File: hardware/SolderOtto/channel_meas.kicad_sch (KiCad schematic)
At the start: 66 parts, among them Q901 BC847A, Q902 BC858B, Q903 BC847A, U901 OPA202, U902 LM358B, U903 74hc4053, U904 OPA202, U905 OPA202

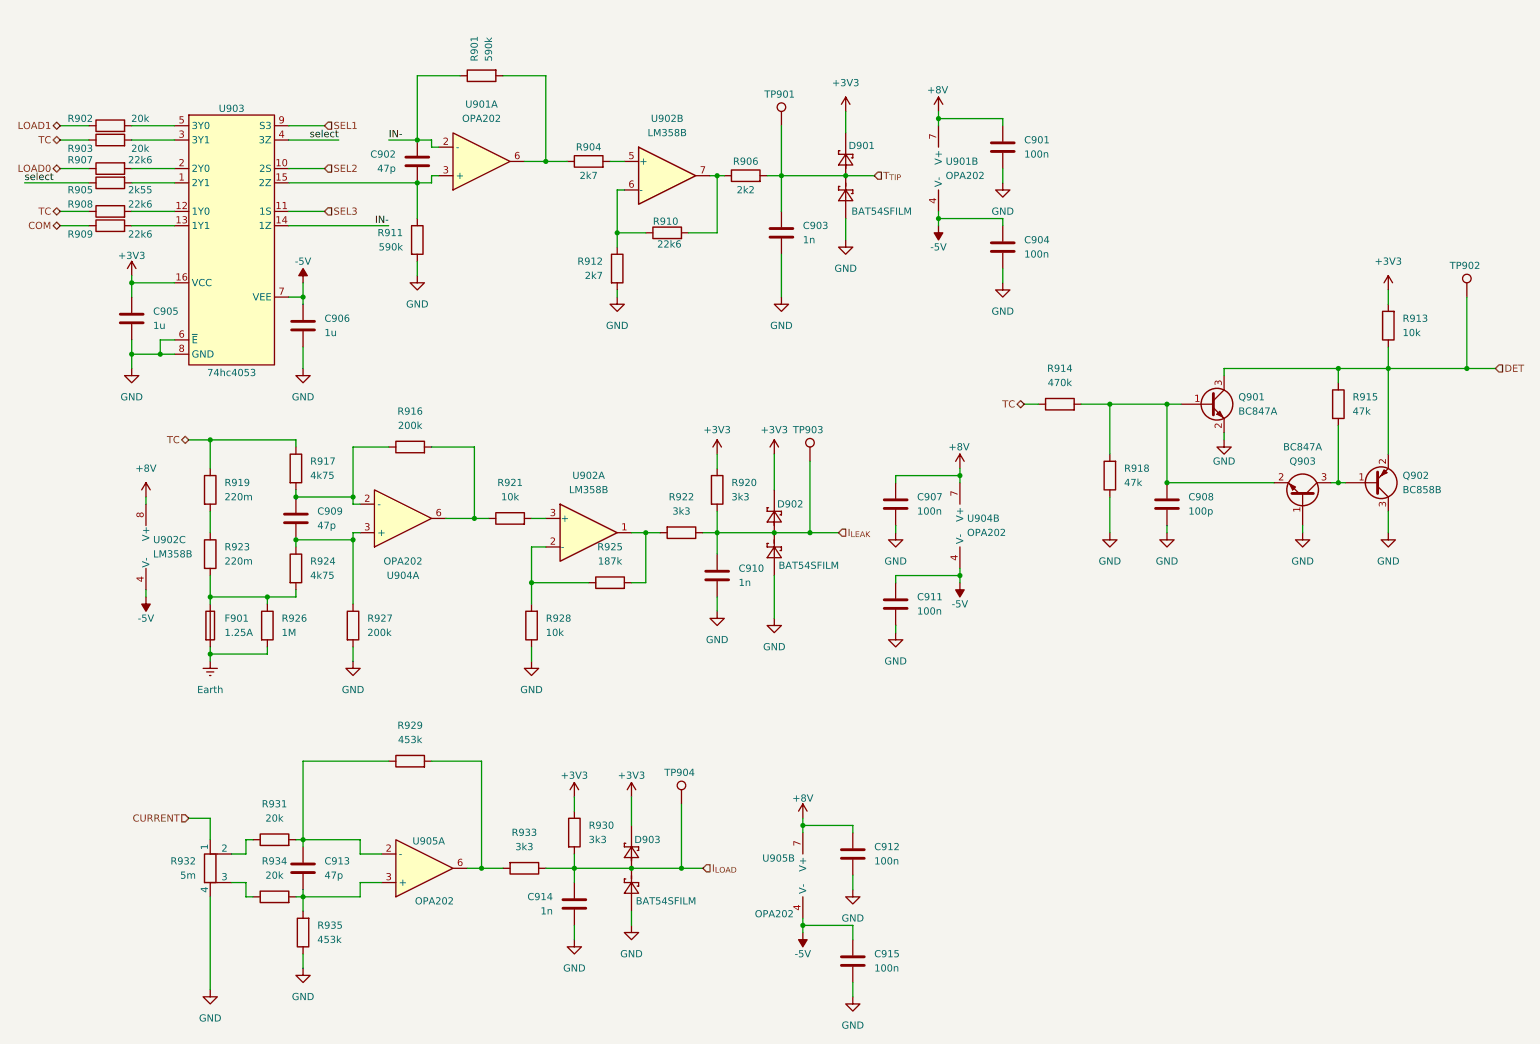
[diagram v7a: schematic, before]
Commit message: rework pcb due to not working one
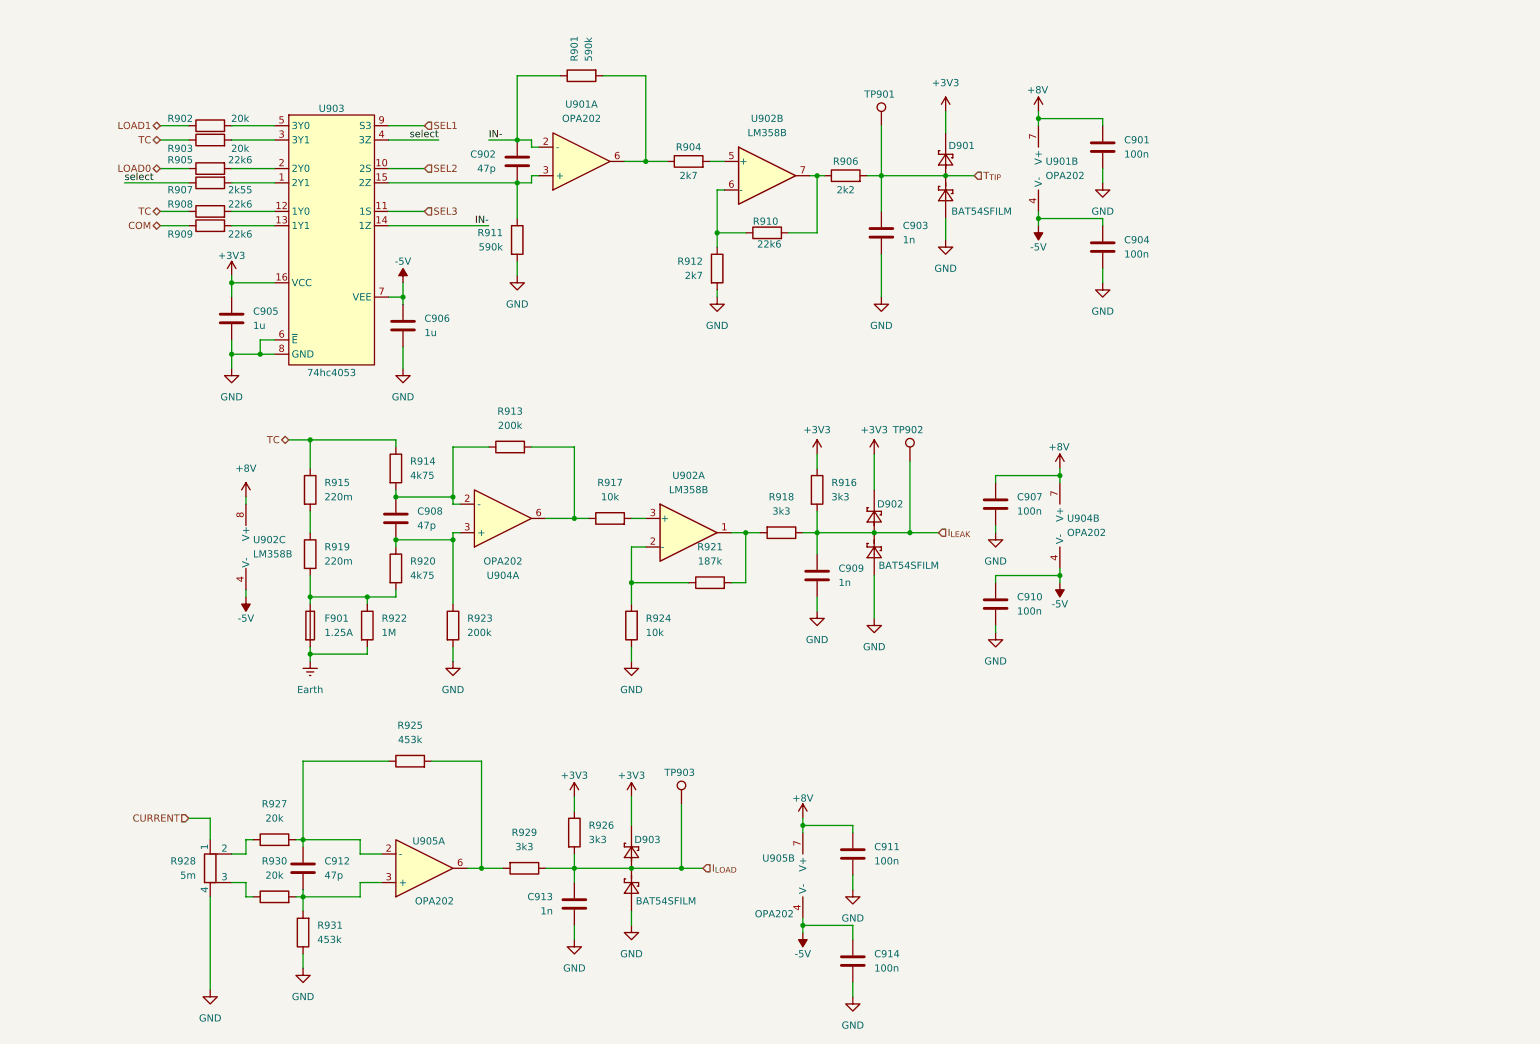
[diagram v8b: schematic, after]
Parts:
- removed C908: 100p, Capacitor_SMD:C_0603_1608Metric, symbol Device:C
- removed Q901, Q903: BC847A, Package_TO_SOT_SMD:SOT-23, symbol Transistor_BJT:BC847
- removed Q902: BC858B, Package_TO_SOT_SMD:SOT-23, symbol Transistor_BJT:BC858
- removed R913: 10k, Resistor_SMD:R_0603_1608Metric, symbol Device:R
- removed R914: 470k, Resistor_SMD:R_0603_1608Metric, symbol Device:R
- removed R915, R918: 47k, Resistor_SMD:R_0603_1608Metric, symbol Device:R
- removed TP902: DET, TestPoint:TestPoint_Keystone_5015_Micro-Minature, symbol Connector:TestPoint
- renumbered C909 to C908, C910 to C909, C911 to C910, C912 to C911, C913 to C912, C914 to C913, C915 to C914, R907 to R905, R905 to R907, R916 to R913, R917 to R914, R919 to R915, R920 to R916, R921 to R917, R922 to R918, R923 to R919, R924 to R920, R925 to R921, R926 to R922, R927 to R923, R928 to R924, R929 to R925, R930 to R926, R931 to R927, R932 to R928, R933 to R929, R934 to R930, R935 to R931, TP903 to TP902, TP904 to TP903
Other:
- moved on the sheet: C901, C902, C903, C904, C905, C906, C907, C908, C909, C910, D901, D902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
